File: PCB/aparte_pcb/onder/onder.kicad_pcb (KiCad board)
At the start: 2 copper layers, 170 x 170 mm, 57 parts

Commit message: pxb
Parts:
- added D1: LED_RGB, LED_SMD:LED_RGB_5050-6, F.Cu at (202.2, 121.8)
- added D10: LED_RGB, LED_SMD:LED_RGB_5050-6, F.Cu at (227.2, 121.8)
- added D11: LED_RGB, LED_SMD:LED_RGB_5050-6, F.Cu at (227.2, 128.3)
- added D12: LED_RGB, LED_SMD:LED_RGB_5050-6, F.Cu at (227.2, 134.9)
- added D2: LED_RGB, LED_SMD:LED_RGB_5050-6, F.Cu at (202.2, 128.3)
- added D3: LED_RGB, LED_SMD:LED_RGB_5050-6, F.Cu at (202.2, 134.9)
- added D4: LED_RGB, LED_SMD:LED_RGB_5050-6, F.Cu at (210.6, 121.8)
- added D5: LED_RGB, LED_SMD:LED_RGB_5050-6, F.Cu at (210.6, 128.3)
- added D6: LED_RGB, LED_SMD:LED_RGB_5050-6, F.Cu at (210.6, 134.9)
- added D7: LED_RGB, LED_SMD:LED_RGB_5050-6, F.Cu at (218.9, 121.8)
- added D8: LED_RGB, LED_SMD:LED_RGB_5050-6, F.Cu at (218.9, 128.3)
- added D9: LED_RGB, LED_SMD:LED_RGB_5050-6, F.Cu at (218.9, 134.9)

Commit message: Add files via upload
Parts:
- added J1: Conn_01x04_Socket, Connector_JST:JST_EH_S4B-EH_1x04_P2.50mm_Horizontal, F.Cu at (59.9, 59.7)
- added J2: Conn_01x10_Socket, Connector_JST:JST_EH_S10B-EH_1x10_P2.50mm_Horizontal, F.Cu at (45.0, 85.5)
- added Q1: NPN, Library:NPN, F.Cu at (77.9, 30.1)
- added Q2: NPN, Library:NPN, F.Cu at (125.0, 24.0)
- added Q3: NPN, Library:NPN, F.Cu at (89.1, 27.0)
- PR1, PR2, PR3, PR4, PR5, PR6, PR7, PR8: footprint Library:FOTORES -> Library:FOTORESist
- moved 220Ω_30 247.2 mm to (24.0, 121.0), turned to -75 degrees
- moved 220Ω_29 245.0 mm to (27.0, 120.0), turned to -75 degrees
- moved 220Ω_33 240.6 mm to (25.0, 76.5), turned to -105 degrees
- moved 220Ω_32 237.6 mm to (28.0, 77.5), turned to -105 degrees
- moved 220Ω_31 234.2 mm to (31.5, 78.0), turned to -105 degrees
- moved 220Ω_36 228.9 mm to (41.0, 49.0), turned to -125 degrees
- moved 220Ω_35 225.4 mm to (43.4, 50.8), turned to -125 degrees
- moved 220Ω_28 222.5 mm to (30.0, 119.0), turned to -75 degrees
- moved 220Ω_34 222.0 mm to (46.0, 52.5), turned to -125 degrees
- moved 220Ω_27 220.4 mm to (36.8, 151.3), turned to -45 degrees
- moved 220Ω_26 218.7 mm to (38.9, 148.9), turned to -45 degrees
- moved D14 217.1 mm to (35.0, 82.0), turned to 70 degrees
- moved 220Ω_25 216.8 mm to (41.3, 146.8), turned to -45 degrees
- moved D13 212.7 mm to (38.3, 83.2), turned to -110 degrees
- moved R2 206.8 mm to (71.4, 30.0), turned to -160 degrees
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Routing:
- net Net-(D14-K): track 0.00 -> 614.5 mm, vias 0 -> 1
- net Net-(D1-BK): track 0.00 -> 548.1 mm, vias 0 -> 41
- net Net-(Q2-E): track 0.00 -> 514.0 mm, vias 0 -> 1
- net Net-(Q1-E): track 0.00 -> 506.8 mm, vias 0 -> 5
- net Net-(Q3-E): track 0.00 -> 484.1 mm, vias 0 -> 2
- net pr4: track 0.00 -> 274.9 mm, vias 0 -> 4
- net pr5: track 0.00 -> 201.9 mm, vias 0 -> 1
- net pr3: track 0.00 -> 196.4 mm, vias 0 -> 2
- net pr6: track 0.00 -> 133.8 mm
- net pr2: track 0.00 -> 131.7 mm, vias 0 -> 4
- net pr1: track 0.00 -> 76.0 mm, vias 0 -> 7
- net ROOD: track 0.00 -> 75.8 mm, vias 0 -> 1
- net BLAUW: track 0.00 -> 64.8 mm, vias 0 -> 1
- net Net-(Q2-B): track 0.00 -> 61.9 mm
- net GROEN: track 0.00 -> 57.0 mm, vias 0 -> 1
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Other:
- outline, holes or cut-outs redrawn

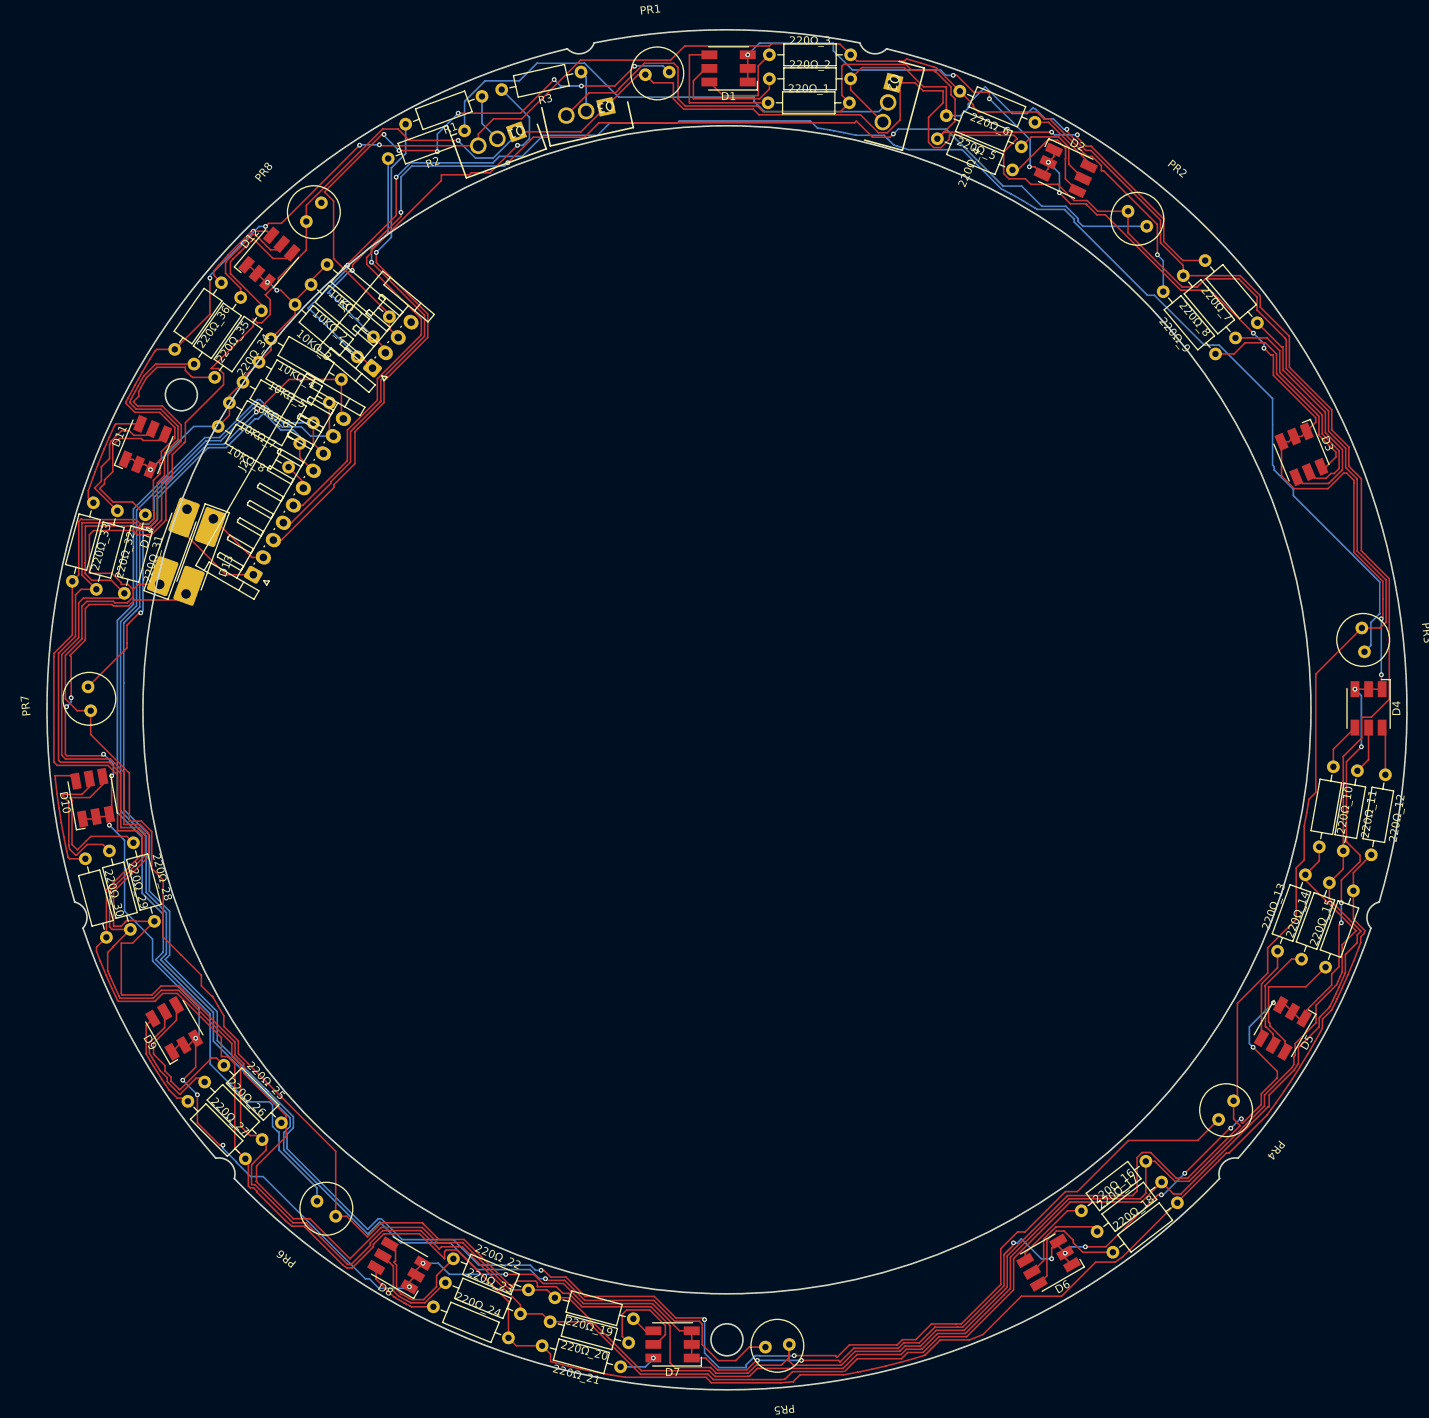
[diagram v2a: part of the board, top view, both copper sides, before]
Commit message: schroef geaard
moet nog onderste schroef
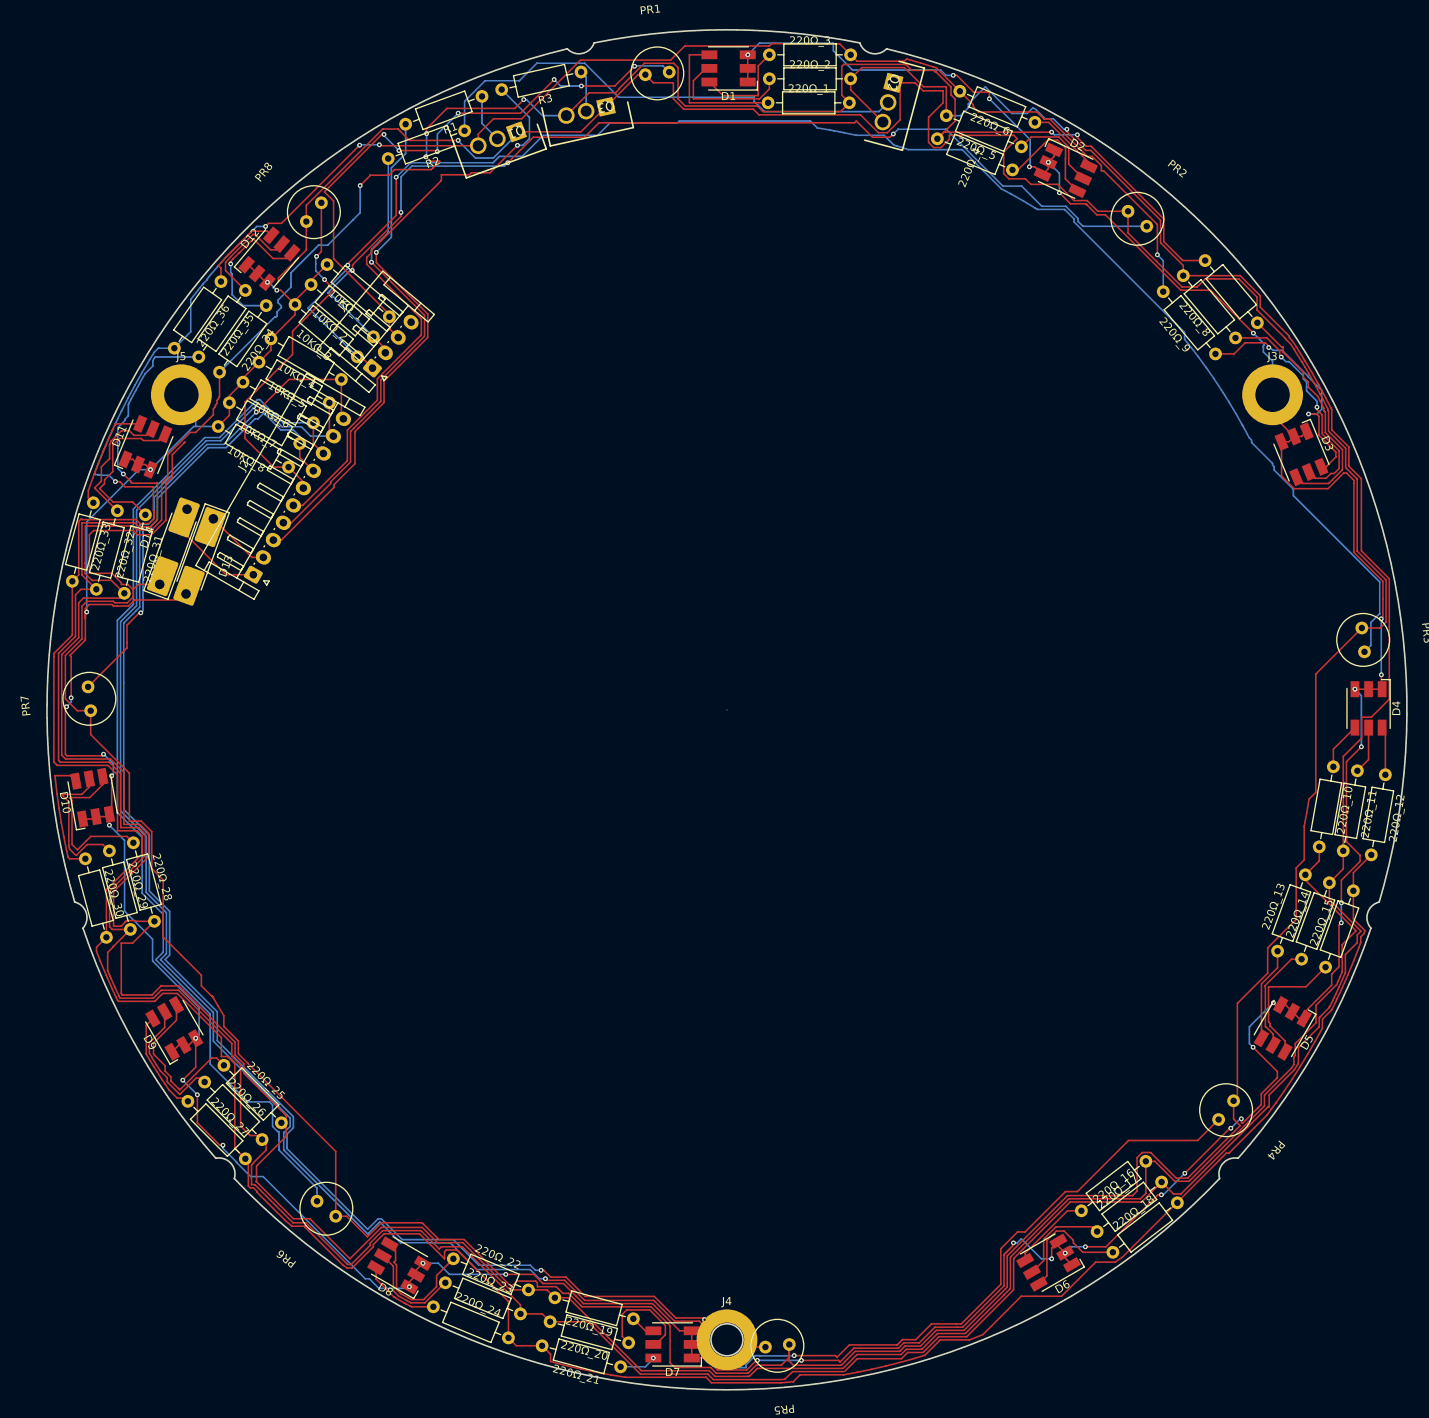
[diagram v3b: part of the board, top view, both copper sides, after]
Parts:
- added J3: Screw_Terminal_01x01, MountingHole:MountingHole_4.3mm_M4_ISO7380_Pad, F.Cu at (172.4, 63.0)
- added J4: Screw_Terminal_01x01, MountingHole:MountingHole_4.3mm_M4_ISO7380_Pad, F.Cu at (104.2, 181.1)
- added J5: Screw_Terminal_01x01, MountingHole:MountingHole_4.3mm_M4_ISO7380_Pad, F.Cu at (36.0, 63.0)
- moved 220Ω_35 1.06 mm to (44.0, 50.0)
- moved 220Ω_34 0.88 mm to (46.6, 51.9)
- moved 220Ω_36 0.16 mm to (41.0, 48.9)
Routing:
- net Net-(Q3-E): track 484.1 -> 540.8 mm, vias 2 -> 6
- net pr8: track 3.39 -> 45.6 mm, vias 0 -> 2
- net Net-(D14-K): track 614.5 -> 585.4 mm
- net Net-(D1-BK): track 548.1 -> 575.0 mm
- net Net-(D3-RA): track 27.1 -> 30.4 mm, vias 0 -> 2
- net pr3: track 196.4 -> 193.9 mm
- net Net-(Q1-E): track 506.8 -> 508.5 mm
- net Net-(D12-BA): track 18.0 -> 19.2 mm, vias 0 -> 1
- net Net-(D12-GA): track 14.7 -> 14.1 mm
- net Net-(D12-RA): track 11.4 -> 10.8 mm
- net Net-(D3-GA): track 28.6 -> 28.8 mm, vias 0 -> 2
- net Net-(Q2-E): track 514.0 -> 513.9 mm, vias 1 -> 2
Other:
- outline, holes or cut-outs redrawn

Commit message: pcb pre autoroute upload
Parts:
- moved R2 124.3 mm to (184.9, 80.6)
- moved R1 122.3 mm to (184.3, 77.6)
- moved R3 122.2 mm to (176.8, 104.4), turned to 102.5 degrees
- moved 10KΩ_2 111.2 mm to (171.0, 61.2)
- moved 10KΩ_3 111.2 mm to (169.0, 63.7)
- moved 10KΩ_8 106.8 mm to (154.9, 55.0)
- moved 10KΩ_7 106.8 mm to (156.3, 52.1)
- moved Q3 101.4 mm to (169.6, 88.5), turned to 120 degrees
- moved 10KΩ_5 98.7 mm to (86.6, 157.4)
- moved 10KΩ_6 98.7 mm to (84.6, 159.9)
- moved 10KΩ_4 98.7 mm to (88.1, 154.4)
- moved Q1 98.5 mm to (163.6, 78.5), turned to 120 degrees
- moved 10KΩ_1 89.6 mm to (65.9, 142.8), turned to -130 degrees
- moved J1 82.9 mm to (77.8, 140.6), turned to 120 degrees
- moved D14 58.8 mm to (58.5, 135.9), turned to 30 degrees
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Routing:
- net Net-(D14-K): track 585.4 -> 0.00 mm, vias 1 -> 0
- net Net-(D1-BK): track 575.0 -> 17.9 mm, vias 41 -> 0
- net Net-(Q3-E): track 540.8 -> 0.00 mm, vias 6 -> 0
- net Net-(Q2-E): track 513.9 -> 0.00 mm, vias 2 -> 0
- net Net-(Q1-E): track 508.5 -> 0.00 mm, vias 5 -> 0
- net pr4: track 274.9 -> 0.00 mm, vias 4 -> 0
- net pr5: track 201.9 -> 0.00 mm, vias 1 -> 0
- net pr3: track 193.9 -> 0.00 mm, vias 2 -> 0
- net pr6: track 133.8 -> 0.00 mm
- net pr2: track 131.7 -> 0.00 mm, vias 4 -> 0
- net pr1: track 76.0 -> 0.00 mm, vias 7 -> 0
- net ROOD: track 75.8 -> 0.00 mm, vias 1 -> 0
- net BLAUW: track 64.8 -> 0.00 mm, vias 1 -> 0
- net Net-(Q2-B): track 61.9 -> 0.00 mm
- net GROEN: track 57.0 -> 0.00 mm, vias 1 -> 0
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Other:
- outline, holes or cut-outs redrawn

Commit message: dgsrf
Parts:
- moved 10KΩ_2 7.09 mm to (166.1, 66.3)
- moved R1 4.05 mm to (182.6, 73.9)
- moved 220Ω_36 3.60 mm to (62.9, 55.0)
- moved 220Ω_35 0.08 mm to (55.8, 51.3)
- turned PR8 to 38 degrees
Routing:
- net Net-(D1-BK): track 17.9 -> 0.00 mm
- net GND: track 10.3 -> 0.00 mm
- net 5V: track 10.2 -> 0.00 mm
- net Net-(D4-RA): track 7.38 -> 0.00 mm
- net Net-(D1-RA): track 7.27 -> 0.00 mm
- net Net-(D9-RA): track 7.15 -> 0.00 mm
- net Net-(D2-GA): track 7.00 -> 0.00 mm
- net Net-(D2-BA): track 6.93 -> 0.00 mm
- net Net-(D2-RA): track 6.89 -> 0.00 mm
- net Net-(D10-BA): track 6.62 -> 0.00 mm
- net Net-(D9-GA): track 6.60 -> 0.00 mm
- net Net-(D1-GA): track 6.27 -> 0.00 mm
- net Net-(D6-RA): track 6.27 -> 0.00 mm
- net Net-(D7-RA): track 6.25 -> 0.00 mm
- net Net-(D3-RA): track 6.17 -> 0.00 mm
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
